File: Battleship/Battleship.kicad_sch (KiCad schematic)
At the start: 0 parts

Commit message: composants kicad
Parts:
- added J1: ecran oled, symbol Connector_Generic:Conn_01x04
- added J2: security, symbol Connector_Generic:Conn_01x02
- added Q1: AO3401A, Package_TO_SOT_SMD:SOT-23, symbol Transistor_FET:AO3401A
- added SW1: bouton_reset, symbol Switch:SW_Push
- added SW2: RotaryEncoder_Switch_horizontal, symbol Device:RotaryEncoder_Switch
- added SW3: RotaryEncoder_Switch_vertical, symbol Device:RotaryEncoder_Switch
- added SW4: bouton_fire, symbol Switch:SW_Push
- added U1: STM32L476RGTx, Package_QFP:LQFP-64_10x10mm_P0.5mm, symbol MCU_ST_STM32L4:STM32L476RGTx
- added U2: AMS1117-3.3, Package_TO_SOT_SMD:SOT-223-3_TabPin2, symbol Regulator_Linear:AMS1117-3.3
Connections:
- new net: U1.18 (VSS), U1.31 (VSS), U1.47 (VSS), U1.63 (VSS)

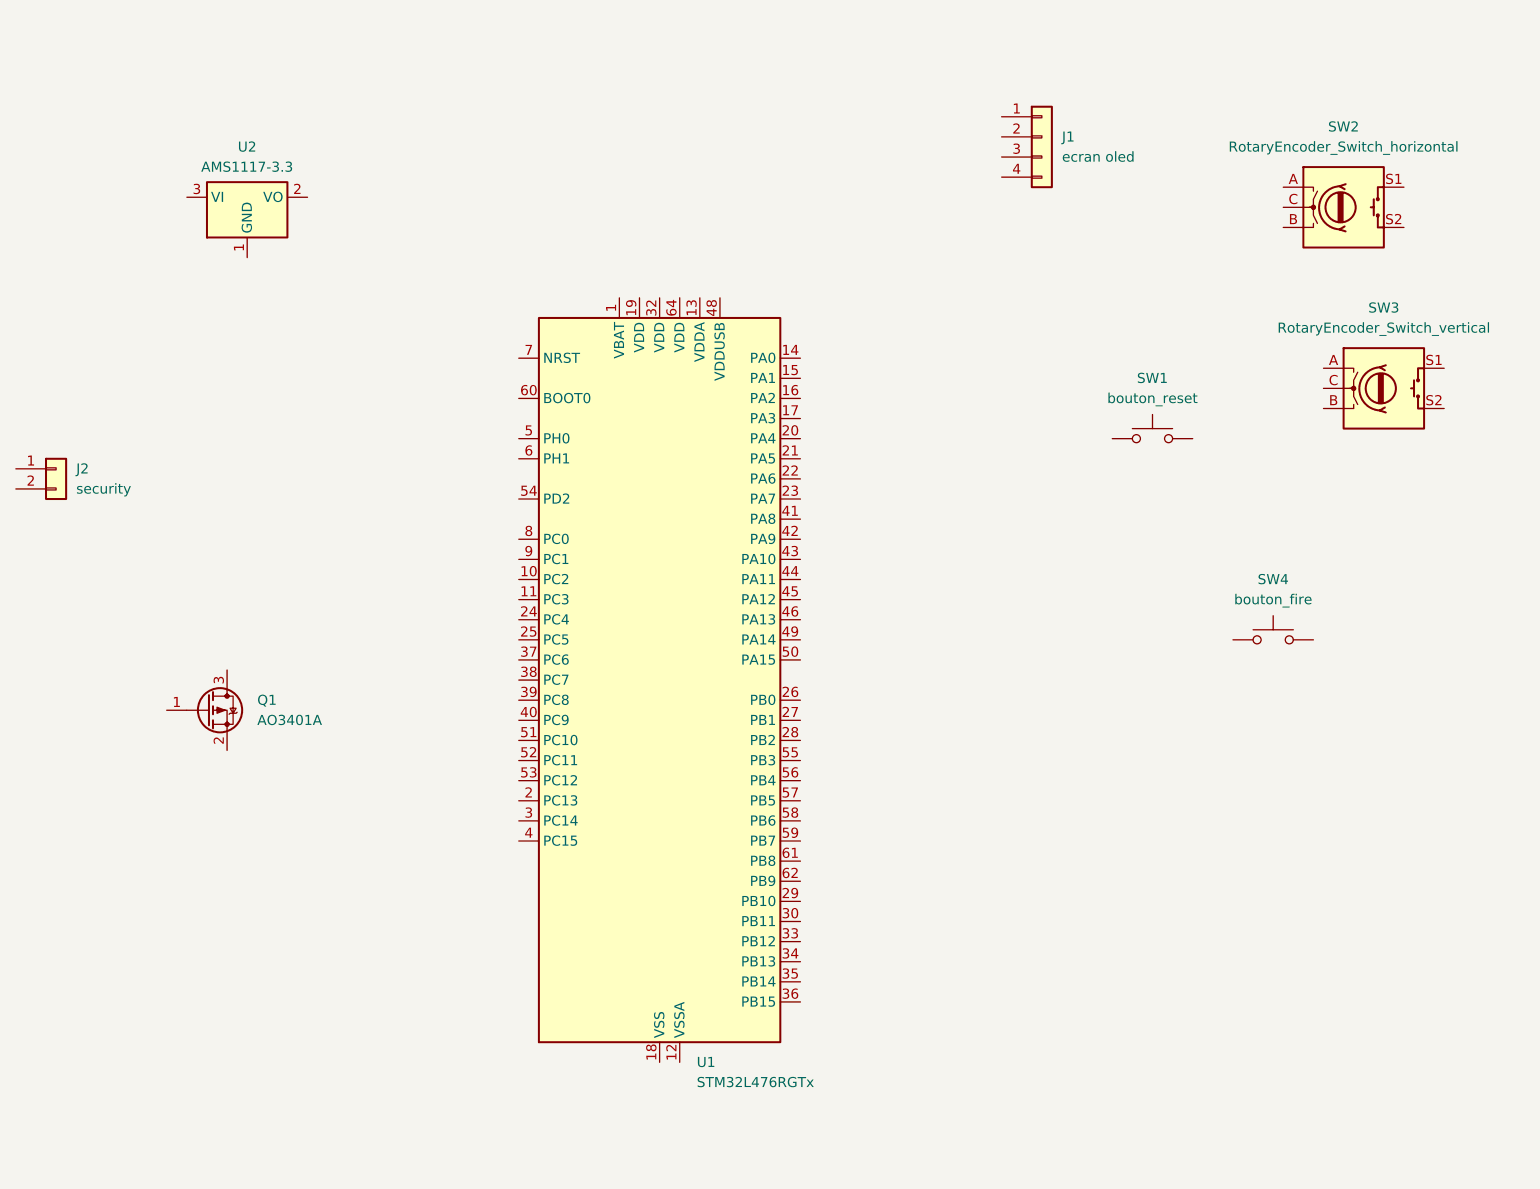
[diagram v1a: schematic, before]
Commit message: ajout de feuilles hiérarchiques
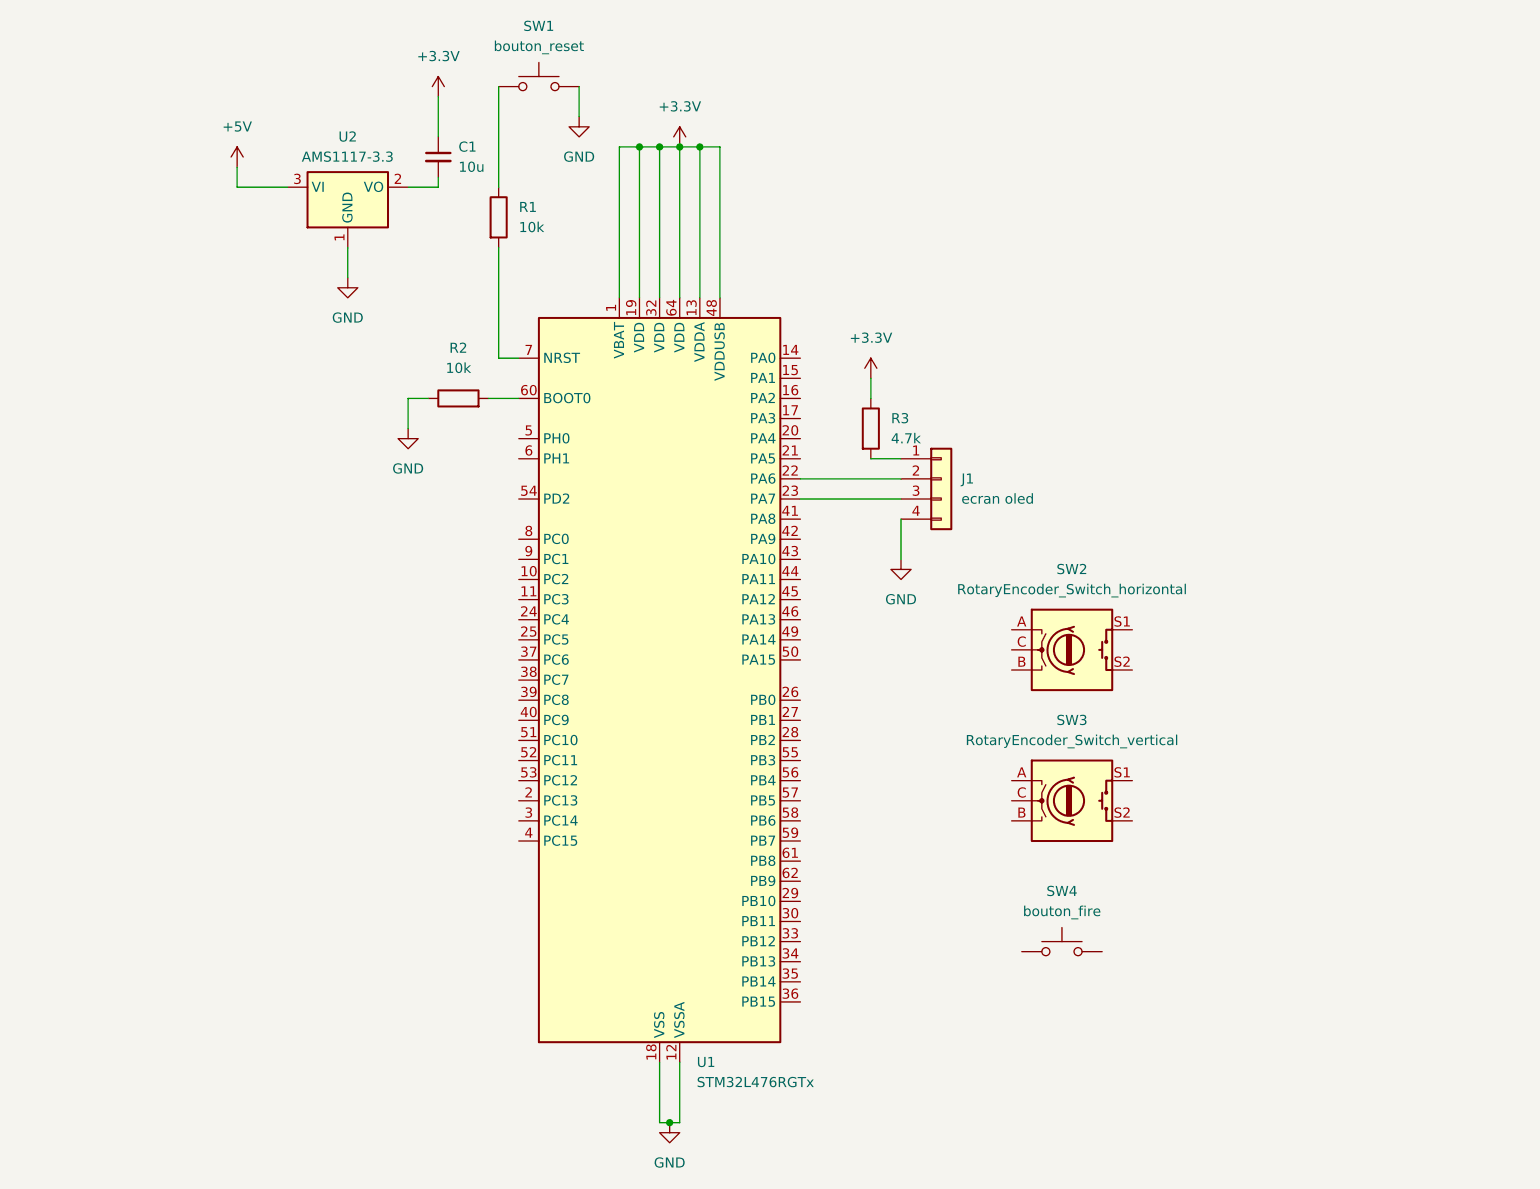
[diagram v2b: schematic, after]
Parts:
- removed J2: security, symbol Connector_Generic:Conn_01x02
- removed Q1: AO3401A, Package_TO_SOT_SMD:SOT-23, symbol Transistor_FET:AO3401A
- added C1: 10u, symbol Device:C_Small
- added R1, R2: 10k, symbol Device:R
- added R3: 4.7k, symbol Device:R
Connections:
- net at SW1.1: now also R1.1
- net GND: now reaches SW1.2
- net GND: now also J1.4 (Pin_4), U1.12 (VSSA), U1.18 (VSS), U1.31 (VSS), U1.47 (VSS), U1.63 (VSS), U2.1 (GND), R2.1
- net at J1.1 (Pin_1): now also R3.2
- net at J1.2 (Pin_2): now also U1.22 (PA6)
- net at J1.3 (Pin_3): now also U1.23 (PA7)
- net at U2.2 (VO): now also C1.2
- net +5V: now reaches U2.3 (VI)
- net +3.3V: now reaches U1.1 (VBAT)
- net +3.3V: now also U1.13 (VDDA), U1.19 (VDD), U1.32 (VDD), U1.48 (VDDUSB), U1.64 (VDD), C1.1, R3.1
- net at U1.60 (BOOT0): now also R2.2
- net at U1.7 (NRST): now also R1.2
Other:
- moved on the sheet: J1, SW1, SW2, SW3, SW4, U2
